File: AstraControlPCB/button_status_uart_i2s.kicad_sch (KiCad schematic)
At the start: 17 parts, among them CN10 JST_ZH_6PIN_1A_250V, CN8 4P JST ZH, CN9 4P JST ZH

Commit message: Updates
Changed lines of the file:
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@@
-	(wire
-		(pts
-			(xy 172.72 83.82) (xy 172.72 106.68)
-		)
-		(stroke
-			(width 0)
-			(type default)
-		)
-	)
 	(wire
 		(pts
@@
 	(wire
 		(pts
-			(xy 175.26 83.82) (xy 175.26 73.66)
+			(xy 172.72 73.66) (xy 172.72 106.68)
 		)
 		(stroke
@@
 	(wire
 		(pts
-			(xy 175.26 73.66) (xy 177.8 73.66)
+			(xy 172.72 73.66) (xy 177.8 73.66)
 		)
 		(stroke
@@
 		)
 		(stroke
-			(width 0)
-			(type default)
-		)
-	)
-	(wire
-		(pts
-			(xy 172.72 83.82) (xy 175.26 83.82)
-		)
-		(stroke

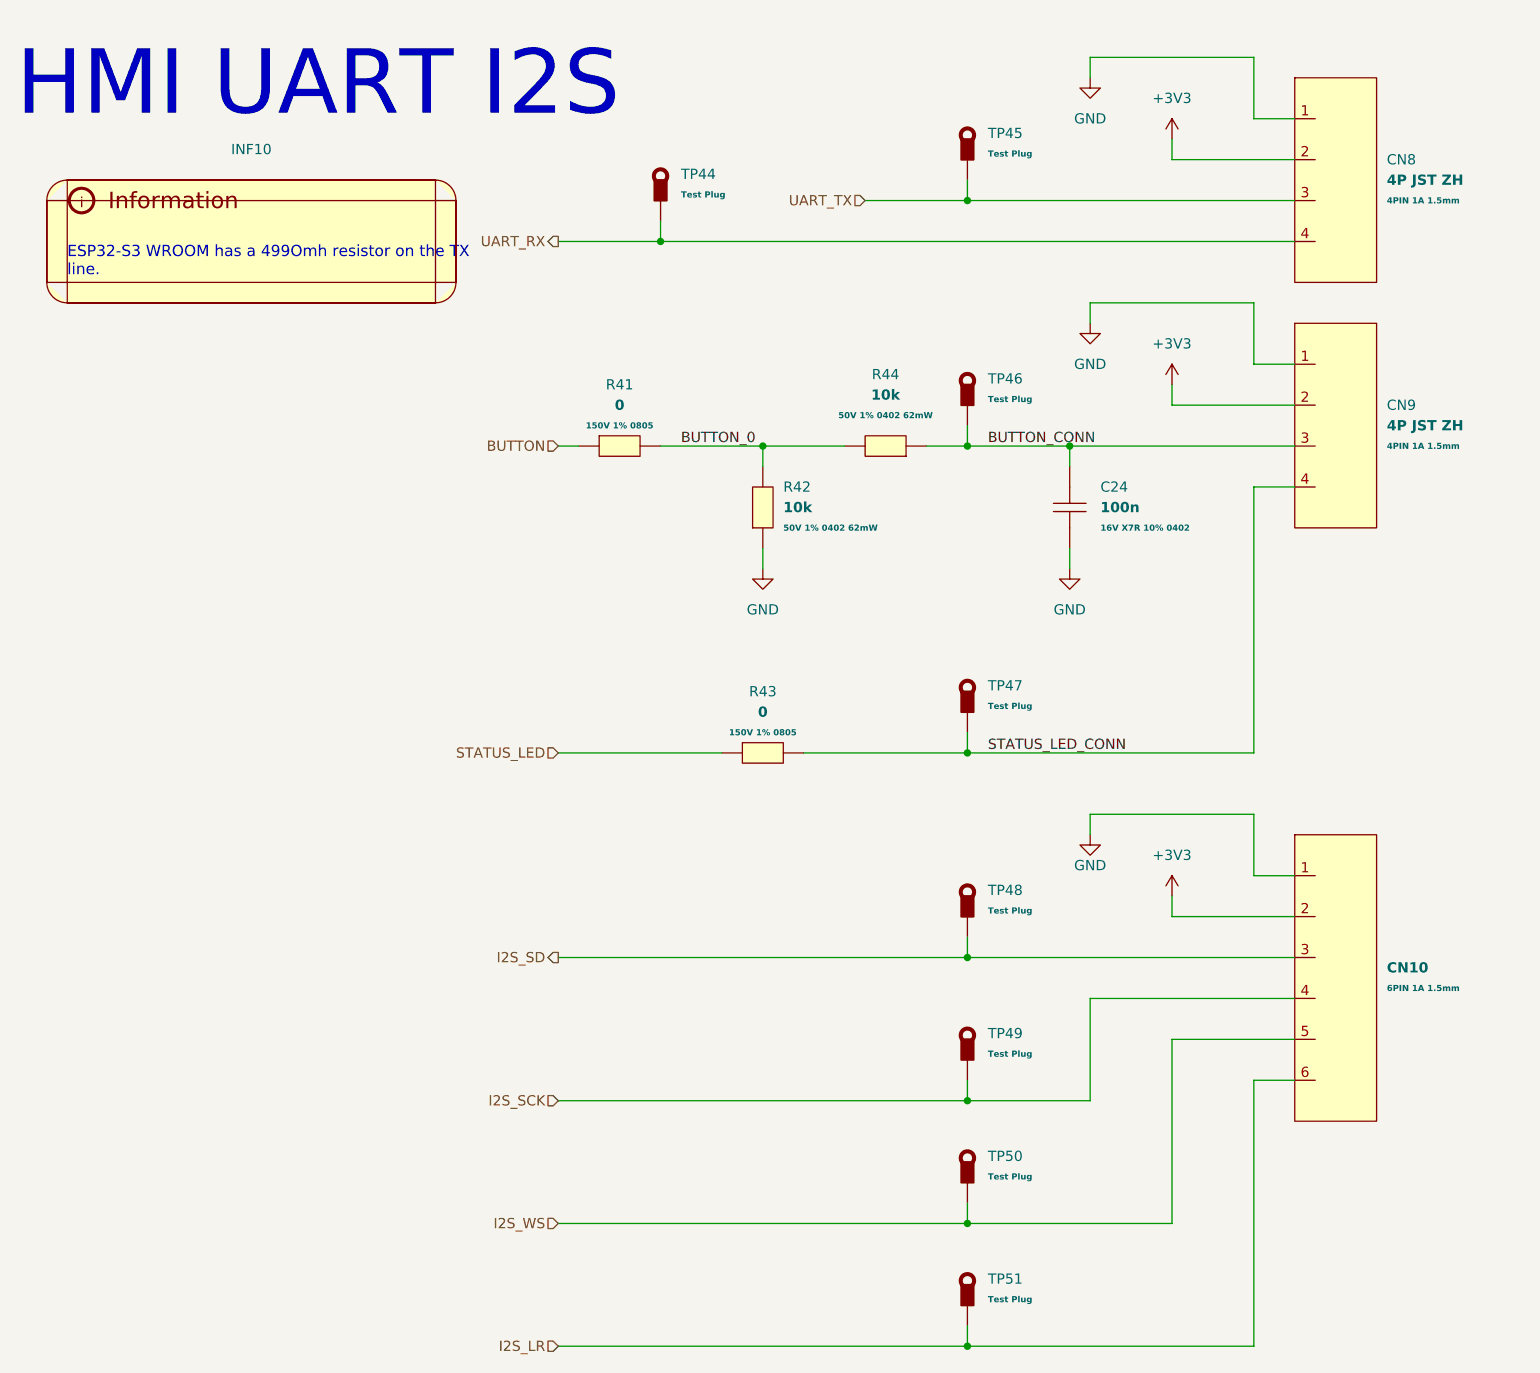
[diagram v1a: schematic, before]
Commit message: Update to new rs485 chip, use 2 bit 5v gpio
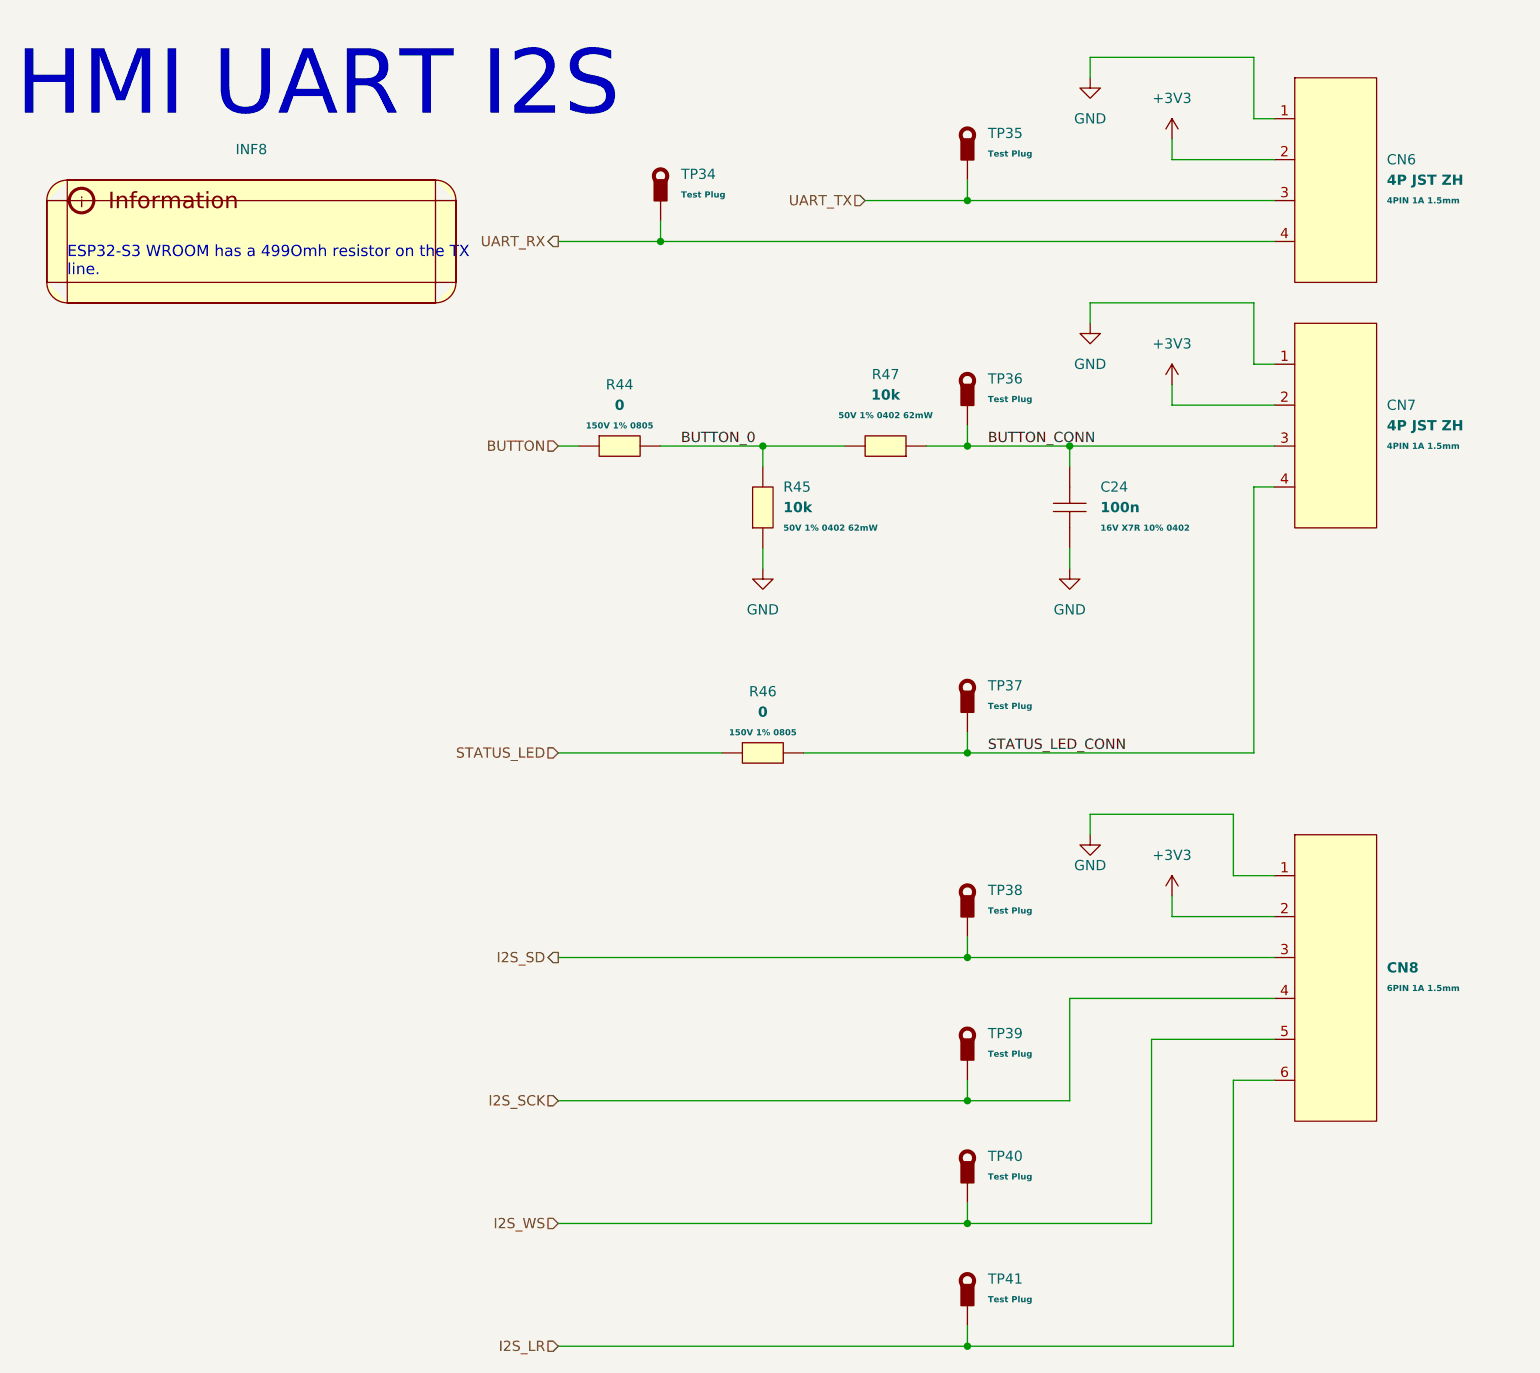
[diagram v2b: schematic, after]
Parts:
- renumbered CN8 to CN6, CN9 to CN7, CN10 to CN8, INF10 to INF8, R41 to R44, R42 to R45, R43 to R46, R44 to R47, TP44 to TP34, TP45 to TP35, TP46 to TP36, TP47 to TP37, TP48 to TP38, TP49 to TP39, TP50 to TP40, TP51 to TP41
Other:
- moved on the sheet: CN6, CN7, CN8

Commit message: New inductor that is in stock, updated rs485 ic layout to put caps closer
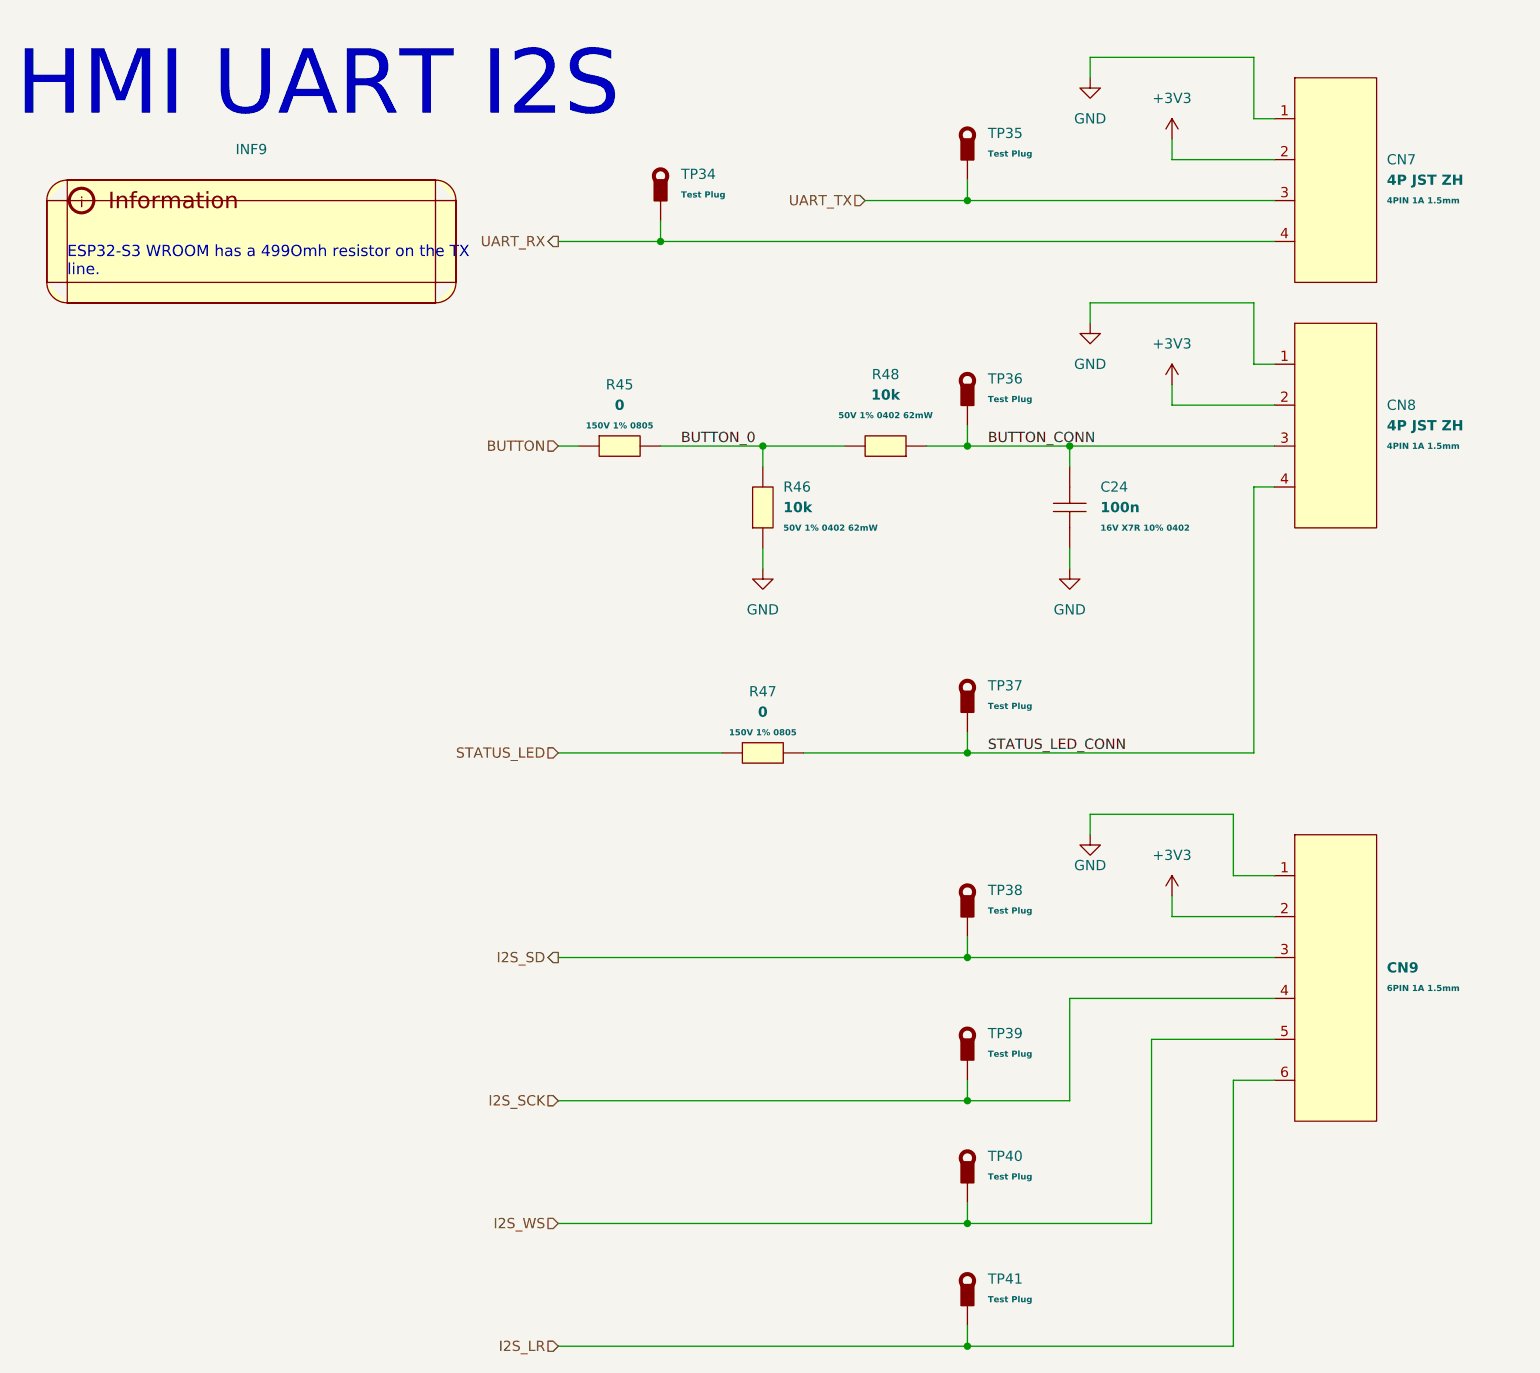
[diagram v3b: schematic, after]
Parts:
- renumbered CN6 to CN7, CN7 to CN8, CN8 to CN9, INF8 to INF9, R44 to R45, R45 to R46, R46 to R47, R47 to R48
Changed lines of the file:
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@@
 		(dnp no)
 		(fields_autoplaced yes)
-		(property "Reference" "CN6"
+		(property "Reference" "CN7"
 			(at 189.23 33.0199 0)
 			(effects
@@
 			(project "AstraControl"
 				(path "/9a751838-dce8-4d69-8a02-736625ac74e7/0db21d8e-3390-4d67-877f-0e5d98e37848/457d2566-de00-4e8c-b469-a22ed41e6193"
-					(reference "CN6")
+					(reference "CN7")
 					(unit 1)
 				)
@@
 		(dnp no)
 		(fields_autoplaced yes)
-		(property "Reference" "#PWR087"
+		(property "Reference" "#PWR090"
 			(at 162.56 64.77 0)
 			(effects
@@
 			(project "AstraControl"
 				(path "/9a751838-dce8-4d69-8a02-736625ac74e7/0db21d8e-3390-4d67-877f-0e5d98e37848/457d2566-de00-4e8c-b469-a22ed41e6193"
-					(reference "#PWR087")
+					(reference "#PWR090")
 					(unit 1)
 				)
@@
 		(dnp no)
 		(fields_autoplaced yes)
-		(property "Reference" "#PWR083"
+		(property "Reference" "#PWR086"
 			(at 152.4 29.21 0)
 			(effects
@@
 			(project "AstraControl"
 				(path "/9a751838-dce8-4d69-8a02-736625ac74e7/0db21d8e-3390-4d67-877f-0e5d98e37848/457d2566-de00-4e8c-b469-a22ed41e6193"
-					(reference "#PWR083")
+					(reference "#PWR086")
 					(unit 1)
 				)
@@
 		(dnp no)
 		(fields_autoplaced yes)
-		(property "Reference" "#PWR084"
+		(property "Reference" "#PWR087"
 			(at 152.4 59.69 0)
 			(effects
@@
 			(project "AstraControl"
 				(path "/9a751838-dce8-4d69-8a02-736625ac74e7/0db21d8e-3390-4d67-877f-0e5d98e37848/457d2566-de00-4e8c-b469-a22ed41e6193"
-					(reference "#PWR084")
+					(reference "#PWR087")
 					(unit 1)
 				)
@@
 		(dnp no)
 		(fields_autoplaced yes)
-		(property "Reference" "#PWR086"
+		(property "Reference" "#PWR089"
 			(at 162.56 34.29 0)
 			(effects
@@
 			(project "AstraControl"
 				(path "/9a751838-dce8-4d69-8a02-736625ac74e7/0db21d8e-3390-4d67-877f-0e5d98e37848/457d2566-de00-4e8c-b469-a22ed41e6193"
-					(reference "#PWR086")
+					(reference "#PWR089")
 					(unit 1)
 				)
@@
 		(on_board yes)
 		(dnp no)
-		(property "Reference" "#PWR085"
+		(property "Reference" "#PWR088"
 			(at 152.4 123.19 0)
 			(effects
@@
 			(project "AstraControl"
 				(path "/9a751838-dce8-4d69-8a02-736625ac74e7/0db21d8e-3390-4d67-877f-0e5d98e37848/457d2566-de00-4e8c-b469-a22ed41e6193"
-					(reference "#PWR085")
+					(reference "#PWR088")
 					(unit 1)
 				)
@@
 		(dnp no)
 		(fields_autoplaced yes)
-		(property "Reference" "R47"
+		(property "Reference" "R48"
 			(at 127 59.69 0)
 			(effects
@@
 			(project "AstraControl"
 				(path "/9a751838-dce8-4d69-8a02-736625ac74e7/0db21d8e-3390-4d67-877f-0e5d98e37848/457d2566-de00-4e8c-b469-a22ed41e6193"
-					(reference "R47")
+					(reference "R48")
 					(unit 1)
 				)
@@
 		(dnp no)
 		(fields_autoplaced yes)
-		(property "Reference" "CN7"
+		(property "Reference" "CN8"
 			(at 189.23 63.4999 0)
 			(effects
@@
 			(project "AstraControl"
 				(path "/9a751838-dce8-4d69-8a02-736625ac74e7/0db21d8e-3390-4d67-877f-0e5d98e37848/457d2566-de00-4e8c-b469-a22ed41e6193"
-					(reference "CN7")
+					(reference "CN8")
 					(unit 1)
 				)
@@
 		(dnp no)
 		(fields_autoplaced yes)
-		(property "Reference" "INF8"
+		(property "Reference" "INF9"
 			(at 48.26 31.75 0)
 			(effects
@@
 			(project ""
 				(path "/9a751838-dce8-4d69-8a02-736625ac74e7/0db21d8e-3390-4d67-877f-0e5d98e37848/457d2566-de00-4e8c-b469-a22ed41e6193"
-					(reference "INF8")
+					(reference "INF9")
 					(unit 1)
 				)
@@
 		(on_board yes)
 		(dnp no)
-		(property "Reference" "R46"
+		(property "Reference" "R47"
 			(at 111.76 99.06 0)
 			(effects
@@
 			(project "AstraControl"
 				(path "/9a751838-dce8-4d69-8a02-736625ac74e7/0db21d8e-3390-4d67-877f-0e5d98e37848/457d2566-de00-4e8c-b469-a22ed41e6193"
-					(reference "R46")
+					(reference "R47")
 					(unit 1)
 				)
@@
 		(dnp no)
 		(fields_autoplaced yes)
-		(property "Reference" "R45"
+		(property "Reference" "R46"
 			(at 114.3 73.6599 90)
 			(effects
@@
 			(project "AstraControl"
 				(path "/9a751838-dce8-4d69-8a02-736625ac74e7/0db21d8e-3390-4d67-877f-0e5d98e37848/457d2566-de00-4e8c-b469-a22ed41e6193"
-					(reference "R45")
+					(reference "R46")
 					(unit 1)
 				)
@@
 		(dnp no)
 		(fields_autoplaced yes)
-		(property "Reference" "#PWR088"
+		(property "Reference" "#PWR091"
 			(at 162.56 128.27 0)
 			(effects
@@
 			(project "AstraControl"
 				(path "/9a751838-dce8-4d69-8a02-736625ac74e7/0db21d8e-3390-4d67-877f-0e5d98e37848/457d2566-de00-4e8c-b469-a22ed41e6193"
-					(reference "#PWR088")
+					(reference "#PWR091")
 					(unit 1)
 				)
@@
 		(dnp no)
 		(fields_autoplaced yes)
-		(property "Reference" "#PWR081"
+		(property "Reference" "#PWR084"
 			(at 111.76 90.17 0)
 			(effects
@@
 			(project "AstraControl"
 				(path "/9a751838-dce8-4d69-8a02-736625ac74e7/0db21d8e-3390-4d67-877f-0e5d98e37848/457d2566-de00-4e8c-b469-a22ed41e6193"
-					(reference "#PWR081")
+					(reference "#PWR084")
 					(unit 1)
 				)
@@
 		(dnp no)
 		(fields_autoplaced yes)
-		(property "Reference" "#PWR082"
+		(property "Reference" "#PWR085"
 			(at 149.86 90.17 0)
 			(effects
@@
 			(project "AstraControl"
 				(path "/9a751838-dce8-4d69-8a02-736625ac74e7/0db21d8e-3390-4d67-877f-0e5d98e37848/457d2566-de00-4e8c-b469-a22ed41e6193"
-					(reference "#PWR082")
+					(reference "#PWR085")
 					(unit 1)
 				)
@@
 		(dnp no)
 		(fields_autoplaced yes)
-		(property "Reference" "CN8"
+		(property "Reference" "CN9"
 			(at 189.23 133.35 0)
 			(effects
@@
 			(project ""
 				(path "/9a751838-dce8-4d69-8a02-736625ac74e7/0db21d8e-3390-4d67-877f-0e5d98e37848/457d2566-de00-4e8c-b469-a22ed41e6193"
-					(reference "CN8")
+					(reference "CN9")
 					(unit 1)
 				)
@@
 		(on_board yes)
 		(dnp no)
-		(property "Reference" "R44"
+		(property "Reference" "R45"
 			(at 93.98 60.96 0)
 			(effects
@@
 			(project "AstraControl"
 				(path "/9a751838-dce8-4d69-8a02-736625ac74e7/0db21d8e-3390-4d67-877f-0e5d98e37848/457d2566-de00-4e8c-b469-a22ed41e6193"
-					(reference "R44")
-					(unit 1)
-				)
+					(reference "R45")
+					(unit 1)
+				)
